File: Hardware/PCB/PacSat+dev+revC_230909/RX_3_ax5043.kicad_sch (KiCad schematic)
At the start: 29 parts, among them U151 RFShield_OnePiece, U405 AX5043

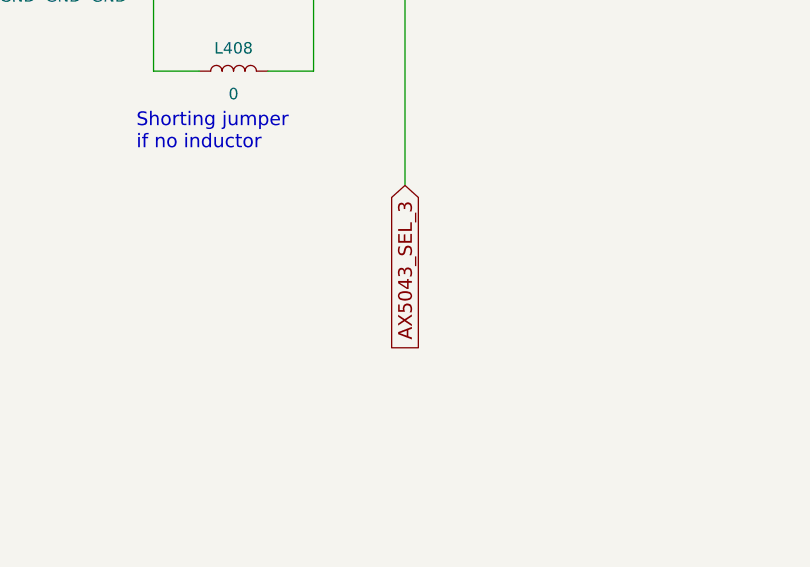
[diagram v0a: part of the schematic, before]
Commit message: Changed schematic to add Select lines for each AX5043 on the CPU.
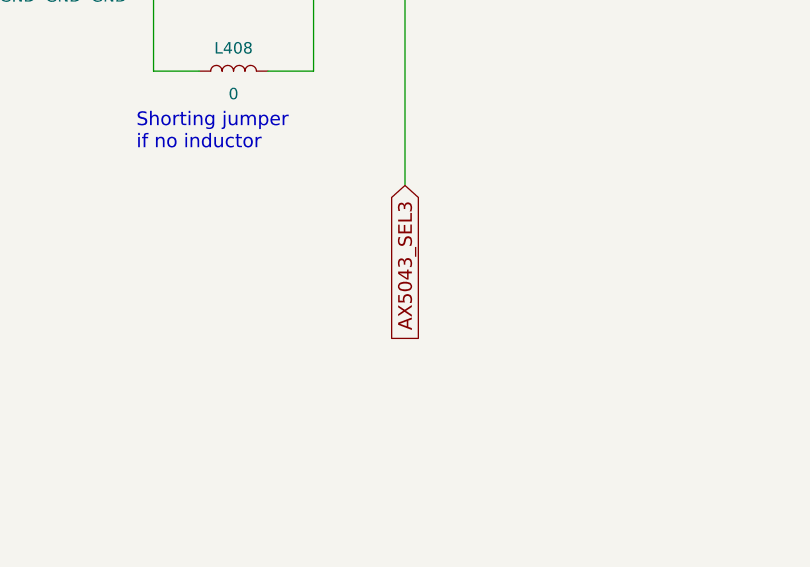
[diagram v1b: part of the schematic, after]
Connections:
- net AX5043_SEL_3 renamed AX5043_SEL3
